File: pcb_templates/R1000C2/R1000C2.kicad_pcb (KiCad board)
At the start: 2 copper layers, 40 x 33.3 mm, 1 part, among them J1 PCIEx1Edge

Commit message: updated template, added libdev schematics
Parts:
- J1: footprint Connect:PCI-EXPRESS -> Main:PCIEXPRESS-X1
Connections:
- J1 pad A1: Net-(J1-PadA1) -> (no net)
- J1 pad B17: Net-(J1-PadB17) -> (no net)
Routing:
- net Net-(J1-PadB9): track 0.00 -> 2.30 mm
- net Net-(J1-PadB8): track 0.00 -> 2.30 mm
- net Net-(J1-PadB7): track 0.00 -> 2.30 mm
- net Net-(J1-PadB6): track 0.00 -> 2.30 mm
- net Net-(J1-PadB5): track 0.00 -> 2.30 mm
- net Net-(J1-PadB4): track 0.00 -> 2.30 mm
- net Net-(J1-PadB3): track 0.00 -> 2.30 mm
- net Net-(J1-PadB2): track 0.00 -> 2.30 mm
- net Net-(J1-PadB18): track 0.00 -> 2.30 mm
- net Net-(J1-PadB16): track 0.00 -> 2.30 mm
- net Net-(J1-PadB15): track 0.00 -> 2.30 mm
- net Net-(J1-PadB14): track 0.00 -> 2.30 mm
- net Net-(J1-PadB13): track 0.00 -> 2.30 mm
- net Net-(J1-PadB12): track 0.00 -> 2.30 mm
- net Net-(J1-PadB11): track 0.00 -> 2.30 mm
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
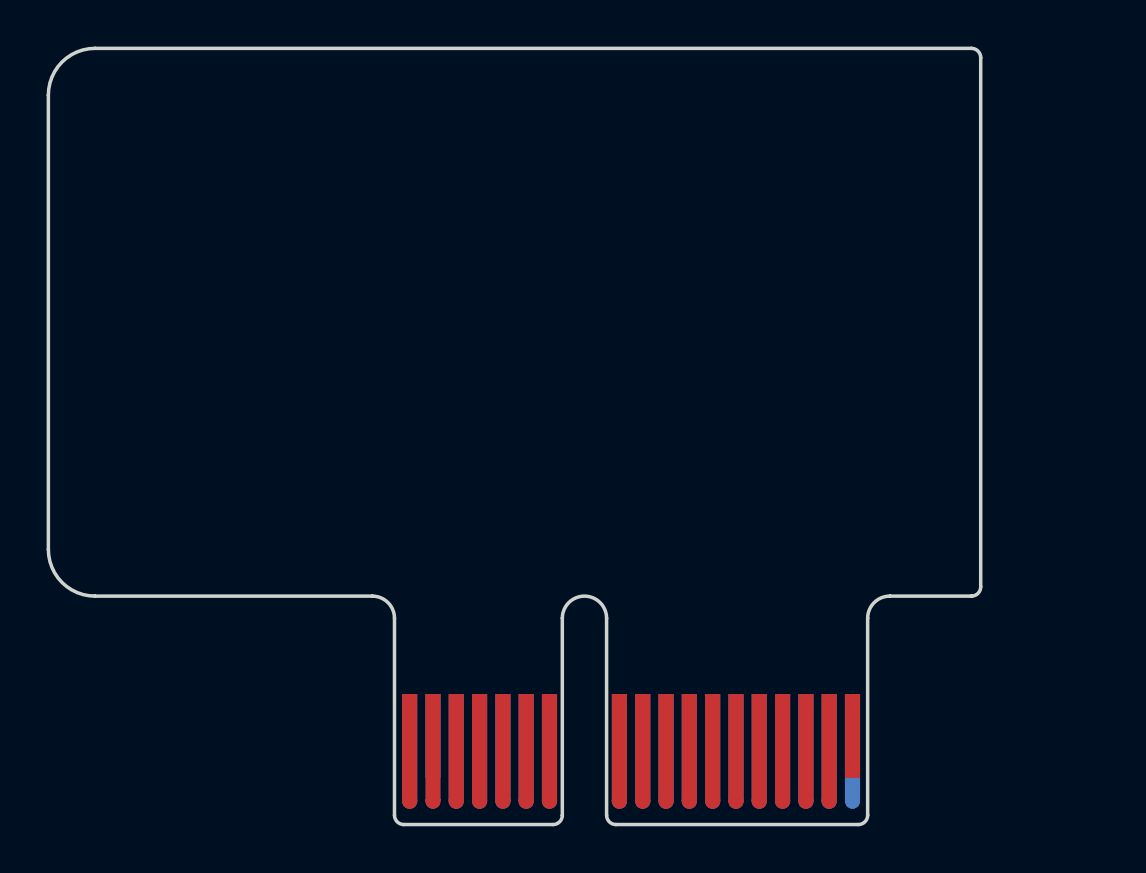
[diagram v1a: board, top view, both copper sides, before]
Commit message: increased PCB boundary to fit a bus bar below, added I2C ID pins and MCU reset to schematic
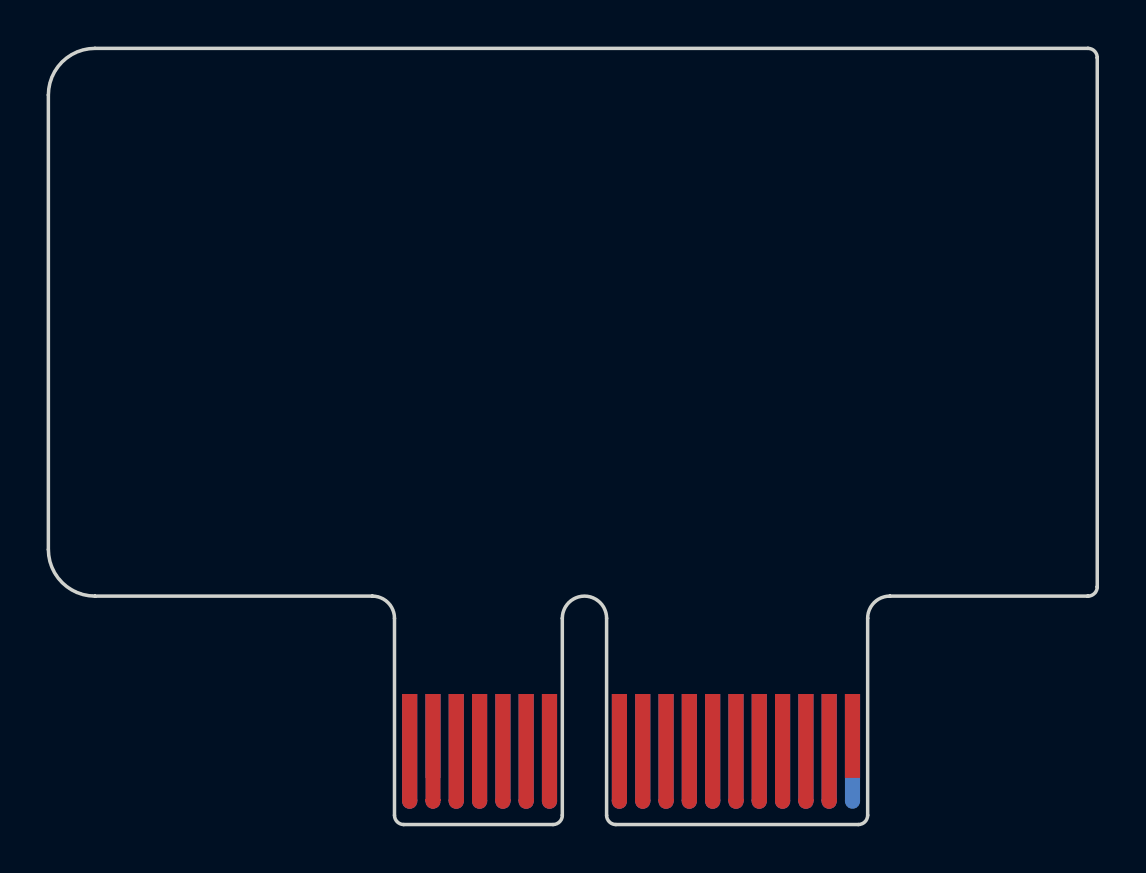
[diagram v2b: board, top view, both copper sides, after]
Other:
- board size 40 x 33.3 mm -> 45 x 33.3 mm
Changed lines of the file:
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@@
     (links 34)
     (no_connects 0)
-    (area 124.924999 69.924999 165.075001 103.375001)
+    (area 124.924999 69.924999 165.075001 103.524461)
     (thickness 1.6)
     (drawings 22)
@@
       (net 18 "Net-(J1-PadA2)"))
   )
-  (gr_arc (start 164.6 70.4) (end 165 70.4) (angle -90) (layer Edge.Cuts) (width 0.15))
-  (gr_arc (start 164.6 93.1) (end 164.6 93.5) (angle -90) (layer Edge.Cuts) (width 0.15))
+  (gr_arc (start 169.6 70.4) (end 170 70.4) (angle -90) (layer Edge.Cuts) (width 0.15))
+  (gr_arc (start 169.6 93.1) (end 169.6 93.5) (angle -90) (layer Edge.Cuts) (width 0.15))
   (gr_arc (start 159.75 102.9) (end 160.15 102.9) (angle 90) (layer Edge.Cuts) (width 0.15))
   (gr_arc (start 149.35 102.9) (end 148.95 102.9) (angle -90) (layer Edge.Cuts) (width 0.15))
   (gr_arc (start 146.65 102.9) (end 147.05 102.9) (angle 90) (layer Edge.Cuts) (width 0.15))
   (gr_arc (start 140.25 102.9) (end 139.85 102.9) (angle -90) (layer Edge.Cuts) (width 0.15))
-  (gr_line (start 165 70.4) (end 165 93.1) (angle 90) (layer Edge.Cuts) (width 0.15))
-  (gr_line (start 164.6 93.5) (end 161.1 93.5) (angle 90) (layer Edge.Cuts) (width 0.15))
+  (gr_line (start 170 70.4) (end 170 93.1) (angle 90) (layer Edge.Cuts) (width 0.15))
+  (gr_line (start 169.6 93.5) (end 161.1 93.5) (angle 90) (layer Edge.Cuts) (width 0.15))
   (gr_arc (start 161.1 94.45) (end 160.15 94.45) (angle 90) (layer Edge.Cuts) (width 0.15))
   (gr_line (start 125 91.5) (end 125 72) (angle 90) (layer Edge.Cuts) (width 0.15))
@@
   (gr_arc (start 138.9 94.45) (end 139.85 94.45) (angle -90) (layer Edge.Cuts) (width 0.15))
   (gr_arc (start 127 72) (end 125 72) (angle 90) (layer Edge.Cuts) (width 0.15))
-  (gr_line (start 164.6 70) (end 127 70) (angle 90) (layer Edge.Cuts) (width 0.15))
+  (gr_line (start 169.6 70) (end 127 70) (angle 90) (layer Edge.Cuts) (width 0.15))
   (gr_line (start 160.15 102.9) (end 160.15 94.45) (angle 90) (layer Edge.Cuts) (width 0.15))
   (gr_line (start 149.35 103.3) (end 159.75 103.3) (angle 90) (layer Edge.Cuts) (width 0.15))
